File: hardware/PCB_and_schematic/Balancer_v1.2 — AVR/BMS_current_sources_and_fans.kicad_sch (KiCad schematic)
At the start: 84 parts, among them J11 HEATSING_TEMP1, J14 LOAD_RESISTOR, J15 LOAD_RESISTOR, J3 Conn_01x03, J4 HEATSING_TEMP1, J5 FAN1, J6 FAN2, J7 BATT_12V, Q10 BC807, Q11 BC817, Q12 BC817, Q13 AO3400A, Q14 BC807, Q15 BC817, Q16 AO3400A, Q18 IRF540N, Q25 IRF540N, Q9 BC817, U1 LM324, U14 LMV358, U2 74AHCT125, U3 74AHCT125

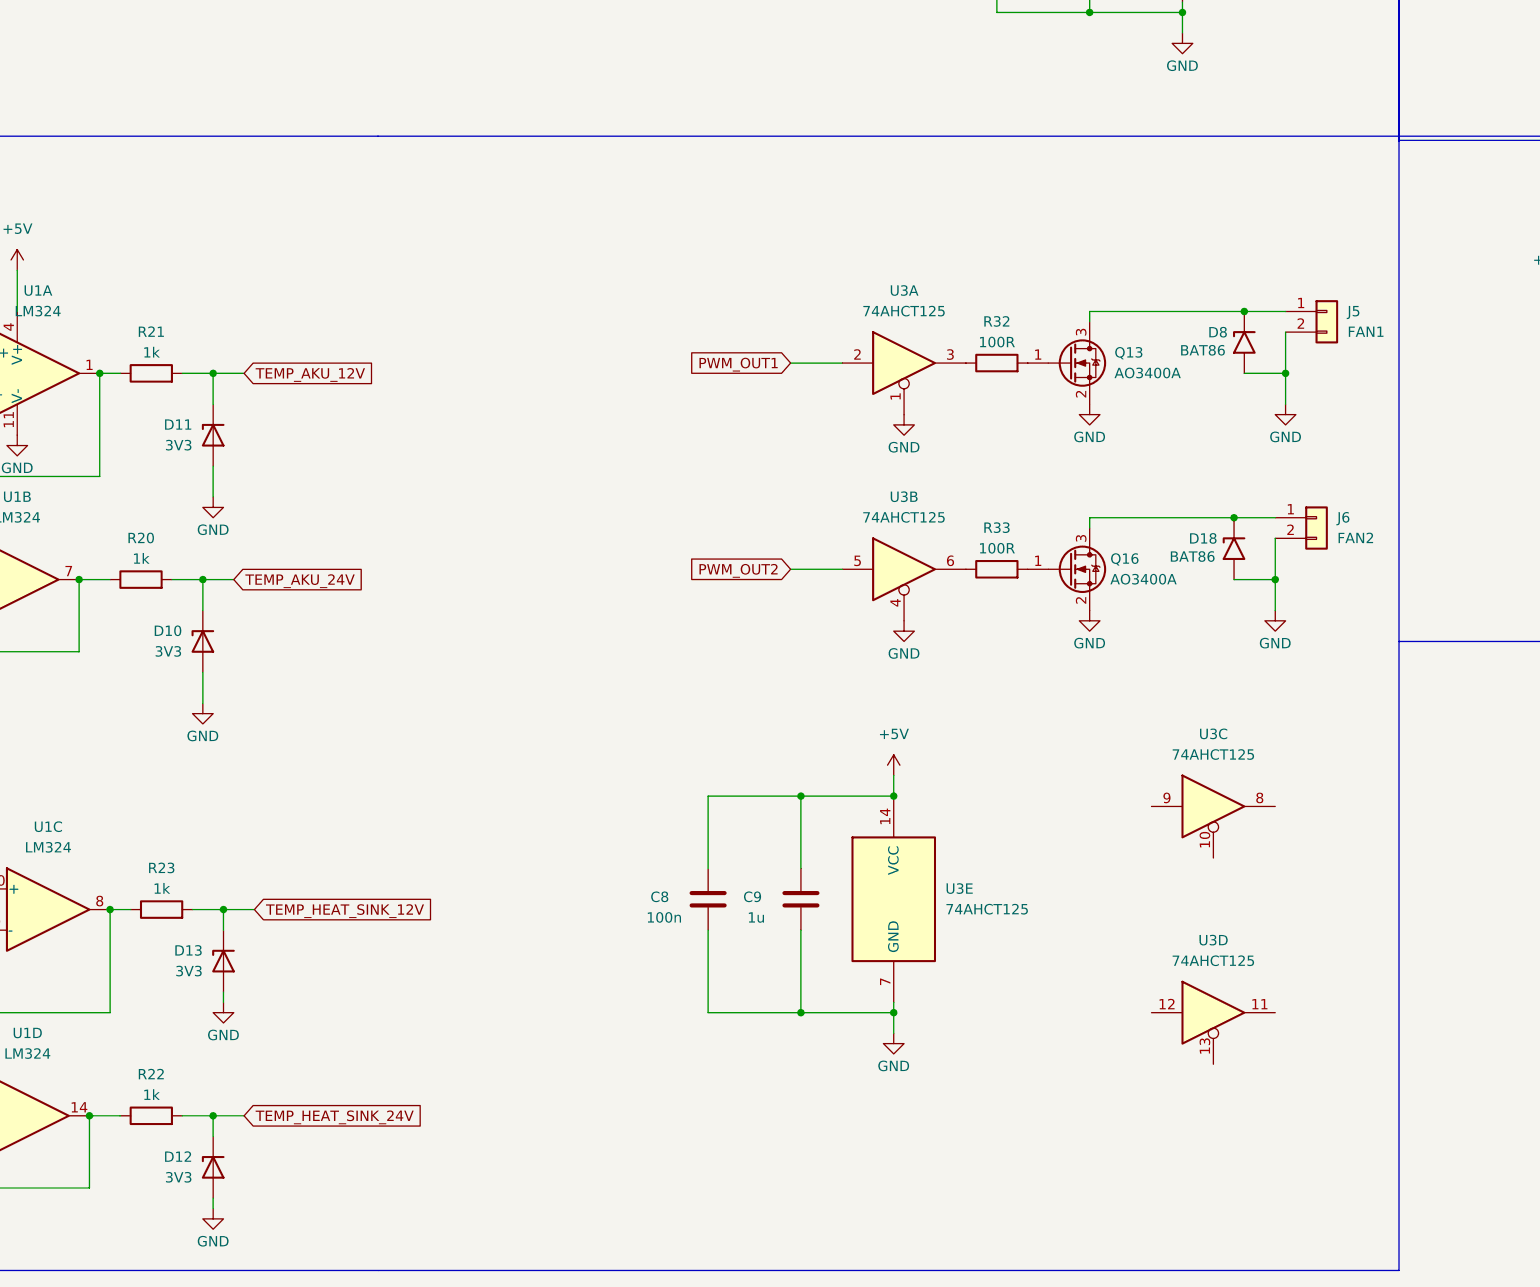
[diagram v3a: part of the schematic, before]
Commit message: mmc pinout update, change schematic
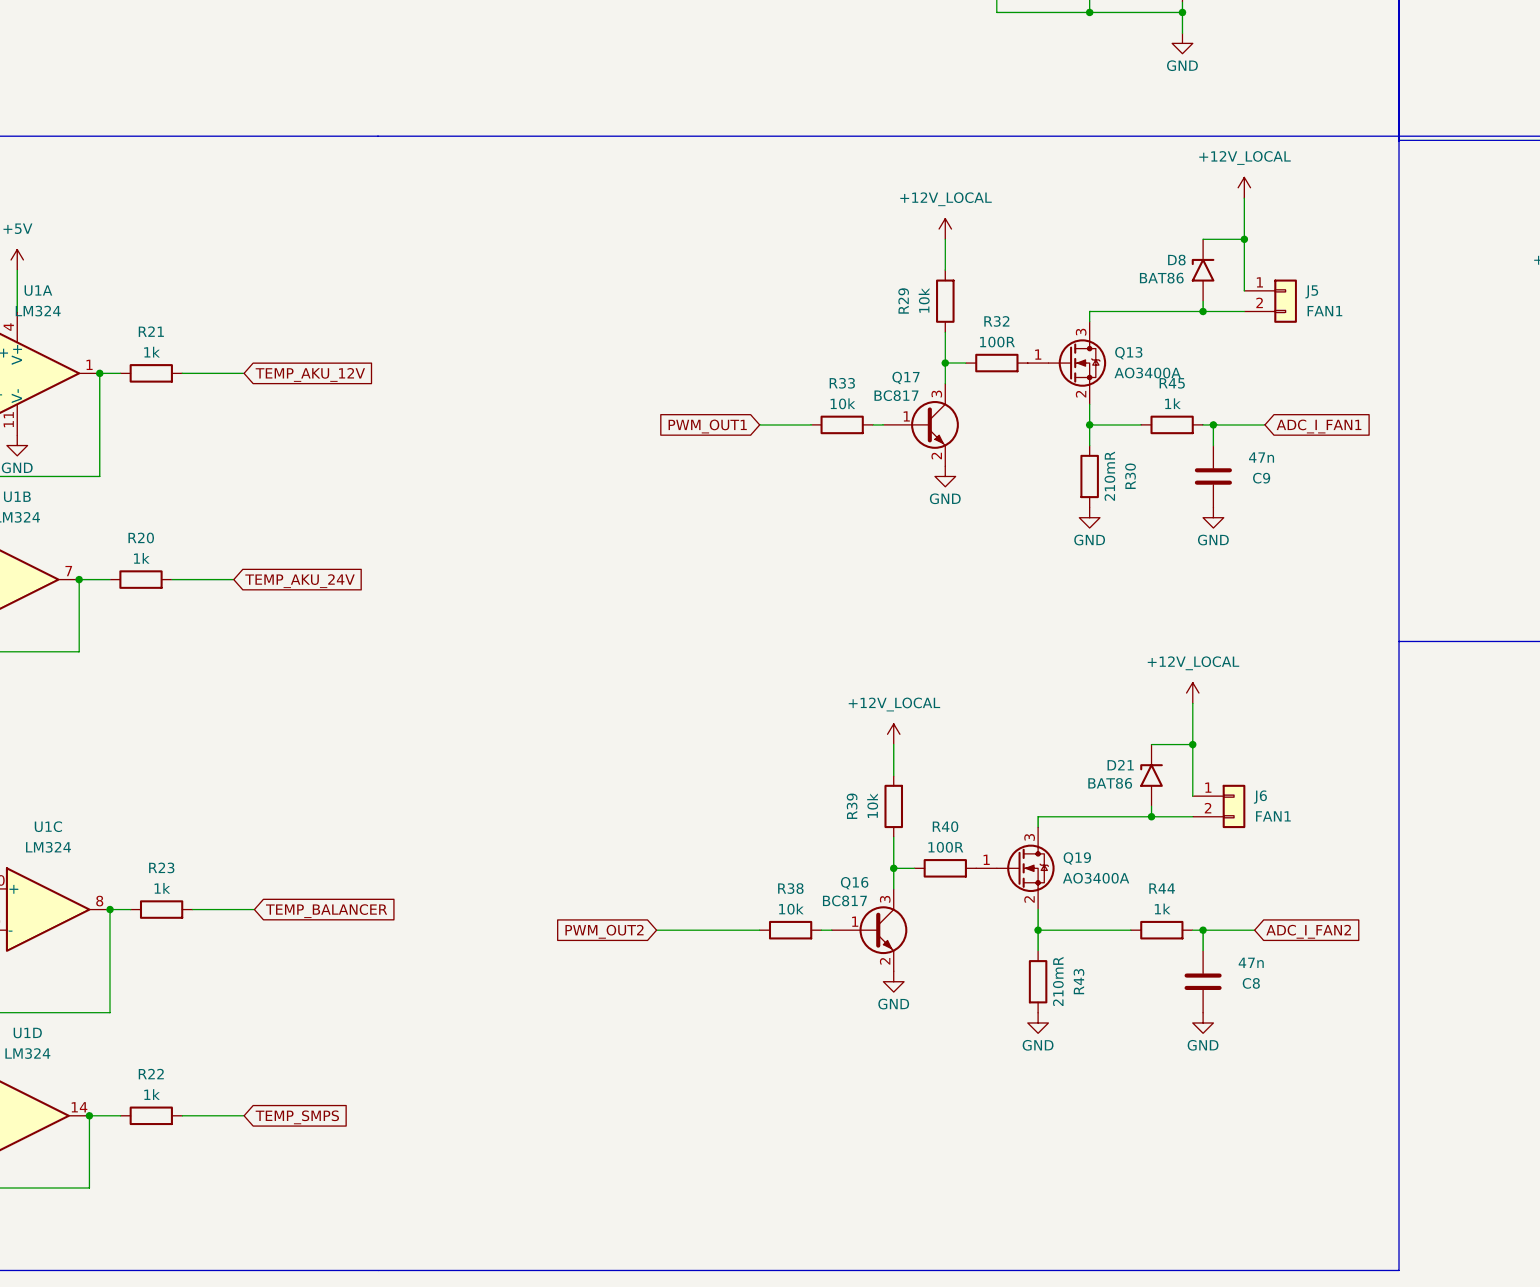
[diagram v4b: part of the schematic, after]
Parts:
- removed D10, D11, D12, D13: 3V3, Diode_SMD:D_MiniMELF, symbol Device:D_Zener
- removed D18: BAT86, Diode_SMD:D_MiniMELF, symbol Diode:SM6T15A
- removed Q16: AO3400A, Package_TO_SOT_SMD:SOT-23, symbol Transistor_FET:AO3400A
- removed U3: 74AHCT125, symbol 74xx:74AHCT125
- added D21: BAT86, Diode_SMD:D_MiniMELF, symbol Diode:SM6T15A
- added Q16, Q17: BC817, Package_TO_SOT_SMD:SOT-23, symbol Transistor_BJT:BC817
- added Q19: AO3400A, Package_TO_SOT_SMD:SOT-23, symbol Transistor_FET:AO3400A
- added R29, R38, R39: 10k, Resistor_SMD:R_0805_2012Metric_Pad1.20x1.40mm_HandSolder, symbol Device:R
- added R30, R43: 210mR, Resistor_SMD:R_0805_2012Metric_Pad1.20x1.40mm_HandSolder, symbol Device:R
- added R40: 100R, Resistor_SMD:R_0805_2012Metric_Pad1.20x1.40mm_HandSolder, symbol Device:R
- added R44, R45: 1k, Resistor_SMD:R_0805_2012Metric_Pad1.20x1.40mm_HandSolder, symbol Device:R
- C8: value 100n -> 47n
- C9: value 1u -> 47n
- J6: value FAN2 -> FAN1
- R33: value 100R -> 10k
- U14: footprint (none) -> Package_SO:SOIC-8_3.9x4.9mm_P1.27mm
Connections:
- net +12V_LOCAL: now also D8.1 (A1), J5.1 (Pin_1), J6.1 (Pin_1), D21.1 (A1), R29.2, R39.2
- net +5V: no longer C8.1, C9.1
- net GND: now also C8.1, C9.1, Q16.2 (E), Q17.2 (E), R30.2, R43.2; no longer C8.2, C9.2, D8.2 (A2), J5.2 (Pin_2), J6.2 (Pin_2), Q13.2 (S)
- net PWM_OUT1: now also R33.1
- net PWM_OUT2: now also R38.1
- net at R33.2: now also Q17.1 (B)
- net at R32.1: now also Q17.3 (C), R29.1
- net TEMP_HEAT_SINK_12V renamed TEMP_BALANCER
- net TEMP_HEAT_SINK_24V renamed TEMP_SMPS
- new net: Q19.2 (S), R43.1, R44.1
- new net: D8.2 (A2), J5.2 (Pin_2), Q13.3 (D)
- new net: D21.2 (A2), J6.2 (Pin_2), Q19.3 (D)
- new net: Q13.2 (S), R30.1, R45.1
- new net: Q16.1 (B), R38.2
- new net: Q16.3 (C), R39.1, R40.1
- new net: Q19.1 (G), R40.2
- new net ADC_I_FAN1: C9.2, R45.2
- new net ADC_I_FAN2: C8.2, R44.2
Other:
- moved on the sheet: D8, J5

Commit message: balancer pcb update
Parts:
- Q18, Q25: footprint Package_TO_SOT_THT:TO-220-3_Vertical -> My-Footprints:TO-220-3_Vertical-little-bigger pads
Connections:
- net PWM_OUT1 renamed PWM_FAN_SMPS
- net PWM_OUT2 renamed PWM_FAN_BALANCER
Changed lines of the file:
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@@
 		)
 	)
-	(global_label "PWM_OUT1"
+	(global_label "PWM_FAN_SMPS"
 		(shape input)
 		(at 194.31 217.17 180)
@@
 		)
 		(property "Intersheetrefs" "${INTERSHEET_REFS}"
-			(at 181.3463 217.17 0)
+			(at 176.5687 217.17 0)
 			(effects
 				(font
@@
 		)
 	)
-	(global_label "PWM_OUT2"
+	(global_label "PWM_FAN_BALANCER"
 		(shape input)
 		(at 181.61 279.4 180)
@@
 		)
 		(property "Intersheetrefs" "${INTERSHEET_REFS}"
-			(at 168.6463 279.4 0)
+			(at 159.5143 279.4 0)
 			(effects
 				(font
@@
 			)
 		)
-		(property "Footprint" "Package_TO_SOT_THT:TO-220-3_Vertical"
+		(property "Footprint" "My-Footprints:TO-220-3_Vertical-little-bigger pads"
 			(at 195.58 116.205 0)
 			(effects
@@
 			)
 		)
-		(property "Footprint" "Package_TO_SOT_THT:TO-220-3_Vertical"
+		(property "Footprint" "My-Footprints:TO-220-3_Vertical-little-bigger pads"
 			(at 430.53 118.745 0)
 			(effects

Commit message: balancer routing done
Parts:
- J11, J4: value HEATSING_TEMP1 -> HEATSINK_TEMP1
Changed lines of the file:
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@@
 			)
 		)
-		(property "Value" "HEATSING_TEMP1"
+		(property "Value" "HEATSINK_TEMP1"
 			(at 52.07 271.78 0)
 			(effects
@@
 			)
 		)
-		(property "Value" "HEATSING_TEMP1"
+		(property "Value" "HEATSINK_TEMP1"
 			(at 52.07 279.4 0)
 			(effects

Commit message: update balancer pcb
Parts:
- J11: value HEATSINK_TEMP1 -> TMP_BALANCER
- J3: value Conn_01x03 -> THERMISTOR_BATT
- J4: value HEATSINK_TEMP1 -> TMP_SMPS
- J5: value FAN1 -> FAN_SMPS
- J6: value FAN1 -> FAN_BALANCER
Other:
- note added: "TEMP-12V"
- note added: "TEMP-24V"
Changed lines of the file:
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@@
 		)
 	)
+	(text "TEMP-12V"
+		(exclude_from_sim no)
+		(at 68.072 213.614 0)
+		(effects
+			(font
+				(size 1.27 1.27)
+			)
+		)
+	)
+	(text "TEMP-24V"
+		(exclude_from_sim no)
+		(at 68.072 216.408 0)
+		(effects
+			(font
+				(size 1.27 1.27)
+			)
+		)
+	)
 	(global_label "TEMP_AKU_24V"
 		(shape input)
@@
 			)
 		)
-		(property "Value" "FAN1"
+		(property "Value" "FAN_BALANCER"
 			(at 255.27 265.4299 0)
 			(effects
@@
 			)
 		)
-		(property "Value" "FAN1"
+		(property "Value" "FAN_SMPS"
 			(at 261.62 203.1999 0)
 			(effects
@@
 			)
 		)
-		(property "Value" "HEATSINK_TEMP1"
+		(property "Value" "TMP_BALANCER"
 			(at 52.07 271.78 0)
 			(effects
@@
 		(on_board yes)
 		(dnp no)
-		(fields_autoplaced yes)
 		(property "Reference" "J3"
-			(at 58.42 209.55 0)
+			(at 58.166 212.09 0)
 			(effects
 				(font
@@
 			)
 		)
-		(property "Value" "Conn_01x03"
-			(at 58.42 212.09 0)
+		(property "Value" "THERMISTOR_BATT"
+			(at 55.118 217.17 90)
 			(effects
 				(font
@@
 			)
 		)
-		(property "Value" "HEATSINK_TEMP1"
+		(property "Value" "TMP_SMPS"
 			(at 52.07 279.4 0)
 			(effects

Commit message: balancer pcb change smps diode footprint, schematic cleanup, designators arrangement, add mouting holes
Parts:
- renumbered C31 to C10, C26 to C11, C8 to C12, C9 to C13, C5 to C14, C6 to C15, C10 to C16, C37 to C17, C39 to C18, C11 to C19, C3 to C5, C29 to C6, C28 to C7, C27 to C8, C30 to C9, D27 to D10, D26 to D11, D21 to D12, D8 to D13, D7 to D14, D14 to D15, D29 to D16, D30 to D17, D31 to D18, D2 to D7, D9 to D8, D28 to D9, J7 to J10, J15 to J11, J11 to J4, J4 to J5, J3 to J6, J14 to J7, J6 to J8, J5 to J9, Q9 to Q10, Q10 to Q11, Q25 to Q12, Q16 to Q13, Q17 to Q14, Q19 to Q15, Q13 to Q16, Q11 to Q17, Q12 to Q18, Q14 to Q19, Q18 to Q20, Q15 to Q9, R13 to R21, R14 to R22, R19 to R23, R16 to R24, R17 to R25, R15 to R26, R20 to R27, R21 to R28, R22 to R29, R23 to R30, R69 to R31, R18 to R32, R70 to R33, R38 to R34, R33 to R35, R81 to R36, R39 to R37, R29 to R38, R40 to R39, R32 to R40, R43 to R41, R30 to R42, R44 to R43, R45 to R44, R24 to R45, R25 to R46, R66 to R47, R67 to R48, R28 to R49, R31 to R50, R34 to R51, R61 to R52, R60 to R53, R62 to R54, R35 to R55, R63 to R56, R71 to R57, U2 to U1, U1 to U2, U14 to U3
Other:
- note added: "BALANCER 12V"
- note added: "BALANCER 24V"
- moved on the sheet: C10, C11, C14, C15, C16, C17, C18, C19, C6, C7, C8, C9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
